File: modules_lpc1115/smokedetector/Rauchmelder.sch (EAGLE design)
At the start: 75 parts, among them IC1 BD9G101, IC2 LPC1115, Q1 BC856, Q3 BCP52, Q4 ASFL, T1 BC847C, T2 BC847C

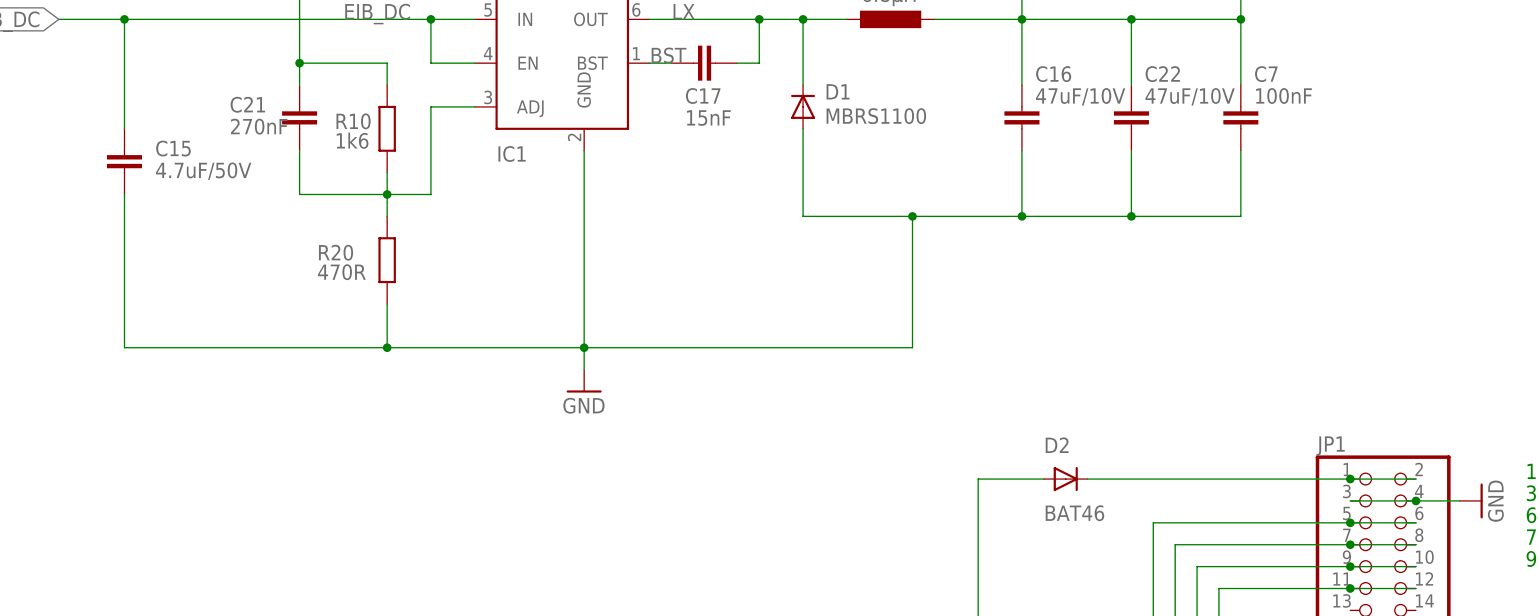
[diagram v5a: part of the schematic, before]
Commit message: [RM] - removed vendor attributes from parts
attributes were not updated and thus were misleading because auf wrong c&p values. So it's better to delete them completely (and perhaps add a dedicated BOM later)
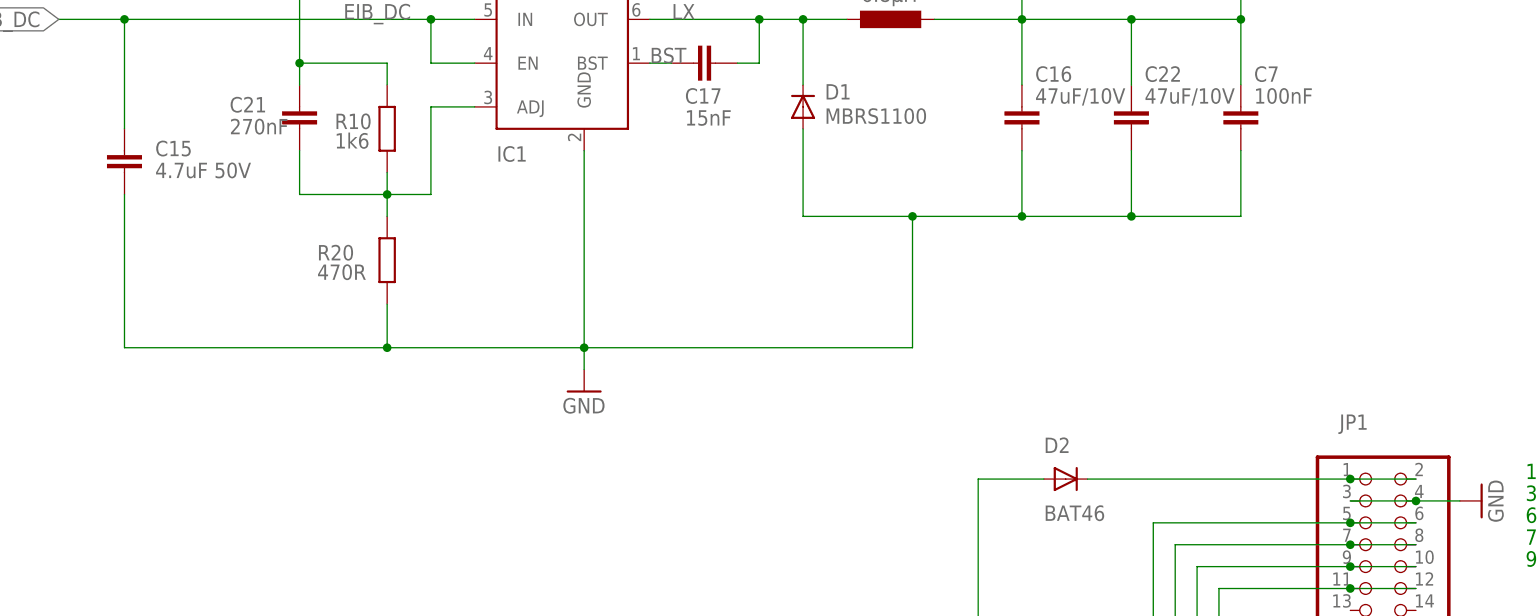
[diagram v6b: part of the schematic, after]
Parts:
- C15: value 4.7uF/50V -> 4.7uF 50V; REICHELT X7R-G1206 4,7/50 -> (none)
- C16, C22: REICHELT X5R-G0805 22/6 -> (none)
- C17: REICHELT X7R-G0805 15N -> (none)
- C21: REICHELT Y5R-G0603 220N -> (none)
- C7: REICHELT X7R-G0805 100N -> (none)
- D1: ALTERNATIVE#1 RB060M-60 -> (none); ALTERNATIVE#2 MBRS1100 -> (none); REICHELT MBRS 1100 SMD -> (none)
- L1: REICHELT L-1616FPS 6,8µ -> (none)
- R10: REICHELT SMD 1/4W 2,4K -> (none)
- R20: REICHELT SMD-0805 680 -> (none)
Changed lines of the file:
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@@
 <part name="C19" library="rcl" library_urn="urn:adsk.eagle:library:334" deviceset="C-EU" device="C0805" package3d_urn="urn:adsk.eagle:package:23617/2" value="1uF"/>
 <part name="GND16" library="supply1" deviceset="GND" device=""/>
-<part name="C7" library="rcl" library_urn="urn:adsk.eagle:library:334" deviceset="C-EU" device="C0805" package3d_urn="urn:adsk.eagle:package:23617/2" value="100nF">
-<attribute name="REICHELT" value="X7R-G0805 100N"/>
-</part>
+<part name="C7" library="rcl" library_urn="urn:adsk.eagle:library:334" deviceset="C-EU" device="C0805" package3d_urn="urn:adsk.eagle:package:23617/2" value="100nF"/>
 <part name="P+2" library="supply1" deviceset="+3V3" device=""/>
 <part name="IC1" library="Stefan_selfbus" deviceset="BD9G101G" device="BD9G101G-SOT23-6" value="BD9G101"/>
-<part name="L1" library="rcl_changed" deviceset="L-EU" device="L4532P" package3d_urn="urn:adsk.eagle:package:23484/1" value="6.8µH">
-<attribute name="REICHELT" value="L-1616FPS 6,8µ"/>
-</part>
-<part name="C15" library="rcl" library_urn="urn:adsk.eagle:library:334" deviceset="C-EU" device="C0805" package3d_urn="urn:adsk.eagle:package:23617/2" value="4.7uF/50V">
-<attribute name="REICHELT" value="X7R-G1206 4,7/50"/>
-</part>
-<part name="C16" library="rcl" library_urn="urn:adsk.eagle:library:334" deviceset="C-EU" device="C0805" package3d_urn="urn:adsk.eagle:package:23617/2" value="47uF/10V">
-<attribute name="REICHELT" value="X5R-G0805 22/6"/>
-</part>
-<part name="C17" library="rcl" library_urn="urn:adsk.eagle:library:334" deviceset="C-EU" device="C1206" package3d_urn="urn:adsk.eagle:package:23618/2" value="15nF">
-<attribute name="REICHELT" value="X7R-G0805 15N"/>
-</part>
-<part name="R10" library="rcl" library_urn="urn:adsk.eagle:library:334" deviceset="R-EU_" device="R0805" package3d_urn="urn:adsk.eagle:package:23553/2" value="1k6">
-<attribute name="REICHELT" value="SMD 1/4W 2,4K"/>
-</part>
-<part name="R20" library="rcl" library_urn="urn:adsk.eagle:library:334" deviceset="R-EU_" device="R0805" package3d_urn="urn:adsk.eagle:package:23553/2" value="470R">
-<attribute name="REICHELT" value="SMD-0805 680"/>
-</part>
-<part name="C21" library="rcl" library_urn="urn:adsk.eagle:library:334" deviceset="C-EU" device="C0805" package3d_urn="urn:adsk.eagle:package:23617/2" value="270nF">
-<attribute name="REICHELT" value="Y5R-G0603 220N"/>
-</part>
-<part name="D1" library="microbuilder" deviceset="DIODE" device="SOD-123" value="MBRS1100">
-<attribute name="ALTERNATIVE#1" value="RB060M-60"/>
-<attribute name="ALTERNATIVE#2" value="MBRS1100"/>
-<attribute name="REICHELT" value="MBRS 1100 SMD"/>
-</part>
+<part name="L1" library="rcl_changed" deviceset="L-EU" device="L4532P" package3d_urn="urn:adsk.eagle:package:23484/1" value="6.8µH"/>
+<part name="C15" library="rcl" library_urn="urn:adsk.eagle:library:334" deviceset="C-EU" device="C0805" package3d_urn="urn:adsk.eagle:package:23617/2" value="4.7uF 50V"/>
+<part name="C16" library="rcl" library_urn="urn:adsk.eagle:library:334" deviceset="C-EU" device="C0805" package3d_urn="urn:adsk.eagle:package:23617/2" value="47uF/10V"/>
+<part name="C17" library="rcl" library_urn="urn:adsk.eagle:library:334" deviceset="C-EU" device="C1206" package3d_urn="urn:adsk.eagle:package:23618/2" value="15nF"/>
+<part name="R10" library="rcl" library_urn="urn:adsk.eagle:library:334" deviceset="R-EU_" device="R0805" package3d_urn="urn:adsk.eagle:package:23553/2" value="1k6"/>
+<part name="R20" library="rcl" library_urn="urn:adsk.eagle:library:334" deviceset="R-EU_" device="R0805" package3d_urn="urn:adsk.eagle:package:23553/2" value="470R"/>
+<part name="C21" library="rcl" library_urn="urn:adsk.eagle:library:334" deviceset="C-EU" device="C0805" package3d_urn="urn:adsk.eagle:package:23617/2" value="270nF"/>
+<part name="D1" library="microbuilder" deviceset="DIODE" device="SOD-123" value="MBRS1100"/>
 <part name="FD1" library="Fiducial" deviceset="FID" device="_40MIL" value="FID_40MIL"/>
 <part name="FD2" library="Fiducial" deviceset="FID" device="_40MIL" value="FID_40MIL"/>
 <part name="FD3" library="Fiducial" deviceset="FID" device="_40MIL" value="FID_40MIL"/>
 <part name="FD4" library="Fiducial" deviceset="FID" device="_40MIL" value="FID_40MIL"/>
-<part name="C22" library="rcl" library_urn="urn:adsk.eagle:library:334" deviceset="C-EU" device="C0805" package3d_urn="urn:adsk.eagle:package:23617/2" value="47uF/10V">
-<attribute name="REICHELT" value="X5R-G0805 22/6"/>
-</part>
+<part name="C22" library="rcl" library_urn="urn:adsk.eagle:library:334" deviceset="C-EU" device="C0805" package3d_urn="urn:adsk.eagle:package:23617/2" value="47uF/10V"/>
 <part name="GND13" library="supply1" deviceset="GND" device=""/>
 <part name="LED2" library="led" library_urn="urn:adsk.eagle:library:259" deviceset="LED" device="CHIPLED_0805" package3d_urn="urn:adsk.eagle:package:15821/2"/>
@@
 </instance>
 <instance part="JP1" gate="A" x="175.26" y="162.56" smashed="yes">
-<attribute name="NAME" x="168.91" y="173.355" size="1.778" layer="95"/>
+<attribute name="NAME" x="171.45" y="175.895" size="1.778" layer="95"/>
 <attribute name="VALUE" x="168.91" y="149.86" size="1.778" layer="96"/>
 </instance>
@@
 </instance>
 <instance part="C7" gate="G$1" x="160.02" y="213.36" smashed="yes" rot="MR0">
-<attribute name="REICHELT" x="160.02" y="213.36" size="1.778" layer="96" rot="MR0" display="off"/>
 <attribute name="NAME" x="161.544" y="218.059" size="1.778" layer="95" rot="MR180"/>
 <attribute name="VALUE" x="161.544" y="215.519" size="1.778" layer="96" rot="MR180"/>
@@
 </instance>
 <instance part="L1" gate="G$1" x="119.38" y="223.52" smashed="yes" rot="R90">
-<attribute name="REICHELT" x="119.38" y="223.52" size="1.778" layer="96" rot="R90" display="off"/>
 <attribute name="NAME" x="116.078" y="228.346" size="1.778" layer="95"/>
 <attribute name="VALUE" x="115.951" y="225.552" size="1.778" layer="96"/>
 </instance>
 <instance part="C15" gate="G$1" x="30.48" y="205.74" smashed="yes" rot="R180">
-<attribute name="REICHELT" x="30.48" y="205.74" size="1.778" layer="96" rot="R180" display="off"/>
 <attribute name="NAME" x="34.036" y="207.645" size="1.778" layer="95"/>
 <attribute name="VALUE" x="34.036" y="205.105" size="1.778" layer="96"/>
 </instance>
 <instance part="C16" gate="G$1" x="134.62" y="213.36" smashed="yes" rot="MR0">
-<attribute name="REICHELT" x="134.62" y="213.36" size="1.778" layer="96" rot="MR0" display="off"/>
 <attribute name="NAME" x="136.144" y="218.059" size="1.778" layer="95" rot="MR180"/>
 <attribute name="VALUE" x="136.144" y="215.519" size="1.778" layer="96" rot="MR180"/>
 </instance>
 <instance part="C17" gate="G$1" x="99.06" y="218.44" smashed="yes" rot="R270">
-<attribute name="REICHELT" x="99.06" y="218.44" size="1.778" layer="96" rot="R270" display="off"/>
 <attribute name="NAME" x="95.504" y="213.741" size="1.778" layer="95"/>
 <attribute name="VALUE" x="95.504" y="211.201" size="1.778" layer="96"/>
 </instance>
 <instance part="R10" gate="G$1" x="60.96" y="210.82" smashed="yes" rot="R90">
-<attribute name="REICHELT" x="60.96" y="210.82" size="1.778" layer="96" rot="R90" display="off"/>
 <attribute name="NAME" x="54.864" y="210.7946" size="1.778" layer="95"/>
 <attribute name="VALUE" x="54.864" y="208.534" size="1.778" layer="96"/>
 </instance>
 <instance part="R20" gate="G$1" x="60.96" y="195.58" smashed="yes" rot="R90">
-<attribute name="REICHELT" x="60.96" y="195.58" size="1.778" layer="96" rot="R90" display="off"/>
 <attribute name="NAME" x="52.832" y="195.5546" size="1.778" layer="95"/>
 <attribute name="VALUE" x="52.832" y="193.294" size="1.778" layer="96"/>
 </instance>
 <instance part="C21" gate="G$1" x="50.8" y="210.82" smashed="yes" rot="R180">
-<attribute name="REICHELT" x="50.8" y="210.82" size="1.778" layer="96" rot="R180" display="off"/>
 <attribute name="NAME" x="42.672" y="212.725" size="1.778" layer="95"/>
 <attribute name="VALUE" x="42.672" y="210.185" size="1.778" layer="96"/>
 </instance>
 <instance part="D1" gate="G$1" x="109.22" y="213.36" smashed="yes" rot="R90">
-<attribute name="REICHELT" x="109.22" y="213.36" size="1.778" layer="96" rot="R90" display="off"/>
 <attribute name="NAME" x="111.7346" y="214.2236" size="1.778" layer="95"/>
 <attribute name="VALUE" x="111.7346" y="211.4042" size="1.778" layer="96"/>
-<attribute name="ALTERNATIVE#1" x="109.22" y="213.36" size="1.778" layer="96" rot="R90" display="off"/>
-<attribute name="ALTERNATIVE#2" x="109.22" y="213.36" size="1.778" layer="96" rot="R90" display="off"/>
 </instance>
 <instance part="FD1" gate="G$2" x="238.76" y="180.34" smashed="yes">
@@
 </instance>
 <instance part="C22" gate="G$1" x="147.32" y="213.36" smashed="yes" rot="MR0">
-<attribute name="REICHELT" x="147.32" y="213.36" size="1.778" layer="96" rot="MR0" display="off"/>
 <attribute name="NAME" x="148.844" y="218.059" size="1.778" layer="95" rot="MR180"/>
 <attribute name="VALUE" x="148.844" y="215.519" size="1.778" layer="96" rot="MR180"/>

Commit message: [RM] - optimized silkscreen
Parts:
- C9: value 330µ -> 330uF
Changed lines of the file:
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@@
 <part name="GND3" library="supply1" deviceset="GND" device=""/>
 <part name="R16" library="rcl" library_urn="urn:adsk.eagle:library:334" deviceset="R-EU_" device="R0805" package3d_urn="urn:adsk.eagle:package:23553/2" value="22k"/>
-<part name="C9" library="rcl" library_urn="urn:adsk.eagle:library:334" deviceset="CPOL-EU" device="E3.5-8" package3d_urn="urn:adsk.eagle:package:23360/2" value="330µ"/>
+<part name="C9" library="rcl" library_urn="urn:adsk.eagle:library:334" deviceset="CPOL-EU" device="E3.5-8" package3d_urn="urn:adsk.eagle:package:23360/2" value="330uF"/>
 <part name="GND17" library="supply1" deviceset="GND" device=""/>
 <part name="D8" library="microbuilder" deviceset="DIODE" device="SOD-123" value="1N4148"/>

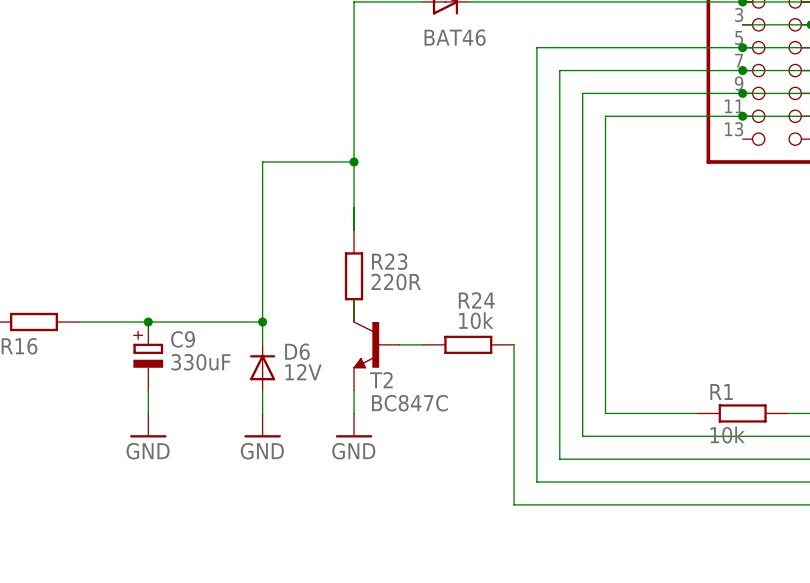
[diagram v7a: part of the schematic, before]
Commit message: [RM] - changed T2 from BC847 to BC817
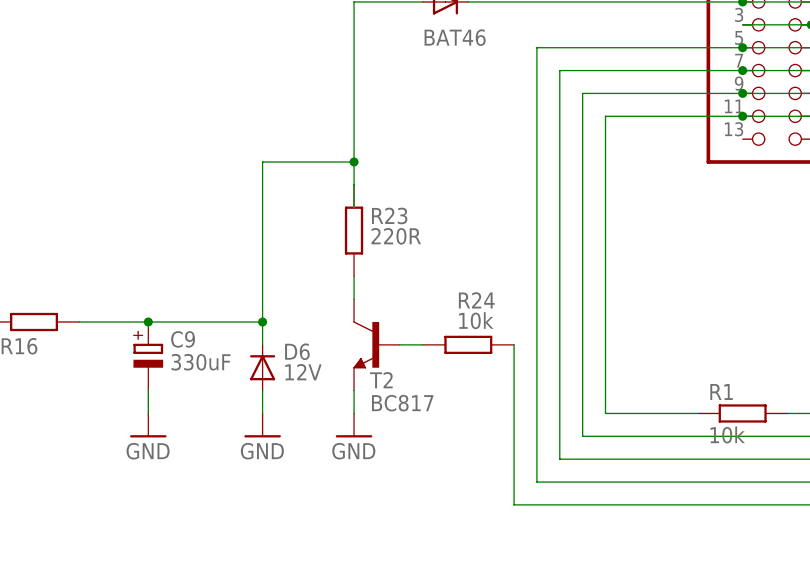
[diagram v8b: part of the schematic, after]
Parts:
- T2: value BC847C -> BC817; device transistor:BC847C -> microbuilder:TRANSISTOR_NPNWIDE
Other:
- moved on the sheet: R23
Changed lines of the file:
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@@
 <part name="LED3" library="led" library_urn="urn:adsk.eagle:library:259" deviceset="LED" device="CHIPLED_0805" package3d_urn="urn:adsk.eagle:package:15821/2"/>
 <part name="R22" library="rcl" library_urn="urn:adsk.eagle:library:334" deviceset="R-EU_" device="R0805" package3d_urn="urn:adsk.eagle:package:23553/2" value="1k"/>
-<part name="T2" library="transistor" deviceset="BC847C" device=""/>
+<part name="T2" library="microbuilder" deviceset="TRANSISTOR_NPN" device="WIDE" value="BC817"/>
 <part name="R23" library="rcl" library_urn="urn:adsk.eagle:library:334" deviceset="R-EU_" device="R2512" package3d_urn="urn:adsk.eagle:package:23545/2" value="220R"/>
 <part name="R24" library="rcl" library_urn="urn:adsk.eagle:library:334" deviceset="R-EU_" device="R0805" package3d_urn="urn:adsk.eagle:package:23553/2" value="10k"/>
@@
 <attribute name="VALUE" x="349.25" y="121.158" size="1.778" layer="96"/>
 </instance>
-<instance part="T2" gate="G$1" x="132.08" y="132.08" smashed="yes" rot="MR0">
+<instance part="T2" gate="G$1" x="129.54" y="132.08" smashed="yes" rot="MR0">
 <attribute name="NAME" x="131.318" y="129.032" size="1.778" layer="95" rot="MR180"/>
 <attribute name="VALUE" x="131.318" y="126.492" size="1.778" layer="96" rot="MR180"/>
 </instance>
-<instance part="R23" gate="G$1" x="129.54" y="139.7" smashed="yes" rot="R270">
-<attribute name="NAME" x="131.318" y="140.4366" size="1.778" layer="95"/>
-<attribute name="VALUE" x="131.318" y="138.176" size="1.778" layer="96"/>
+<instance part="R23" gate="G$1" x="129.54" y="144.78" smashed="yes" rot="R270">
+<attribute name="NAME" x="131.318" y="145.5166" size="1.778" layer="95"/>
+<attribute name="VALUE" x="131.318" y="143.256" size="1.778" layer="96"/>
 </instance>
 <instance part="R24" gate="G$1" x="142.24" y="132.08" smashed="yes">
@@
 <wire x1="119.38" y1="134.62" x2="119.38" y2="152.4" width="0.1524" layer="91"/>
 <wire x1="129.54" y1="170.18" x2="137.16" y2="170.18" width="0.1524" layer="91"/>
-<wire x1="129.54" y1="147.32" x2="129.54" y2="144.78" width="0.1524" layer="91"/>
-<wire x1="129.54" y1="144.78" x2="129.54" y2="152.4" width="0.1524" layer="91"/>
+<wire x1="129.54" y1="147.32" x2="129.54" y2="149.86" width="0.1524" layer="91"/>
+<wire x1="129.54" y1="149.86" x2="129.54" y2="152.4" width="0.1524" layer="91"/>
 <pinref part="R23" gate="G$1" pin="1"/>
 <wire x1="119.38" y1="152.4" x2="129.54" y2="152.4" width="0.1524" layer="91"/>
@@
 <pinref part="R23" gate="G$1" pin="2"/>
 <pinref part="T2" gate="G$1" pin="C"/>
-<wire x1="129.54" y1="137.16" x2="129.54" y2="134.62" width="0.1524" layer="91"/>
+<wire x1="129.54" y1="137.16" x2="129.54" y2="139.7" width="0.1524" layer="91"/>
 </segment>
 </net>
@@
 <pinref part="T2" gate="G$1" pin="B"/>
 <pinref part="R24" gate="G$1" pin="1"/>
-<wire x1="137.16" y1="132.08" x2="134.62" y2="132.08" width="0.1524" layer="91"/>
-</segment>
-</net>
+<wire x1="134.62" y1="132.08" x2="137.16" y2="132.08" width="0.1524" layer="91"/>
+</segment>
+</net>
